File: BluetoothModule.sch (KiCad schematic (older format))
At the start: 21 parts, among them J8 SW_DIP_x01, J9 SW_DIP_x01, U17 BM64SPKS1MCx, U5 APX803L

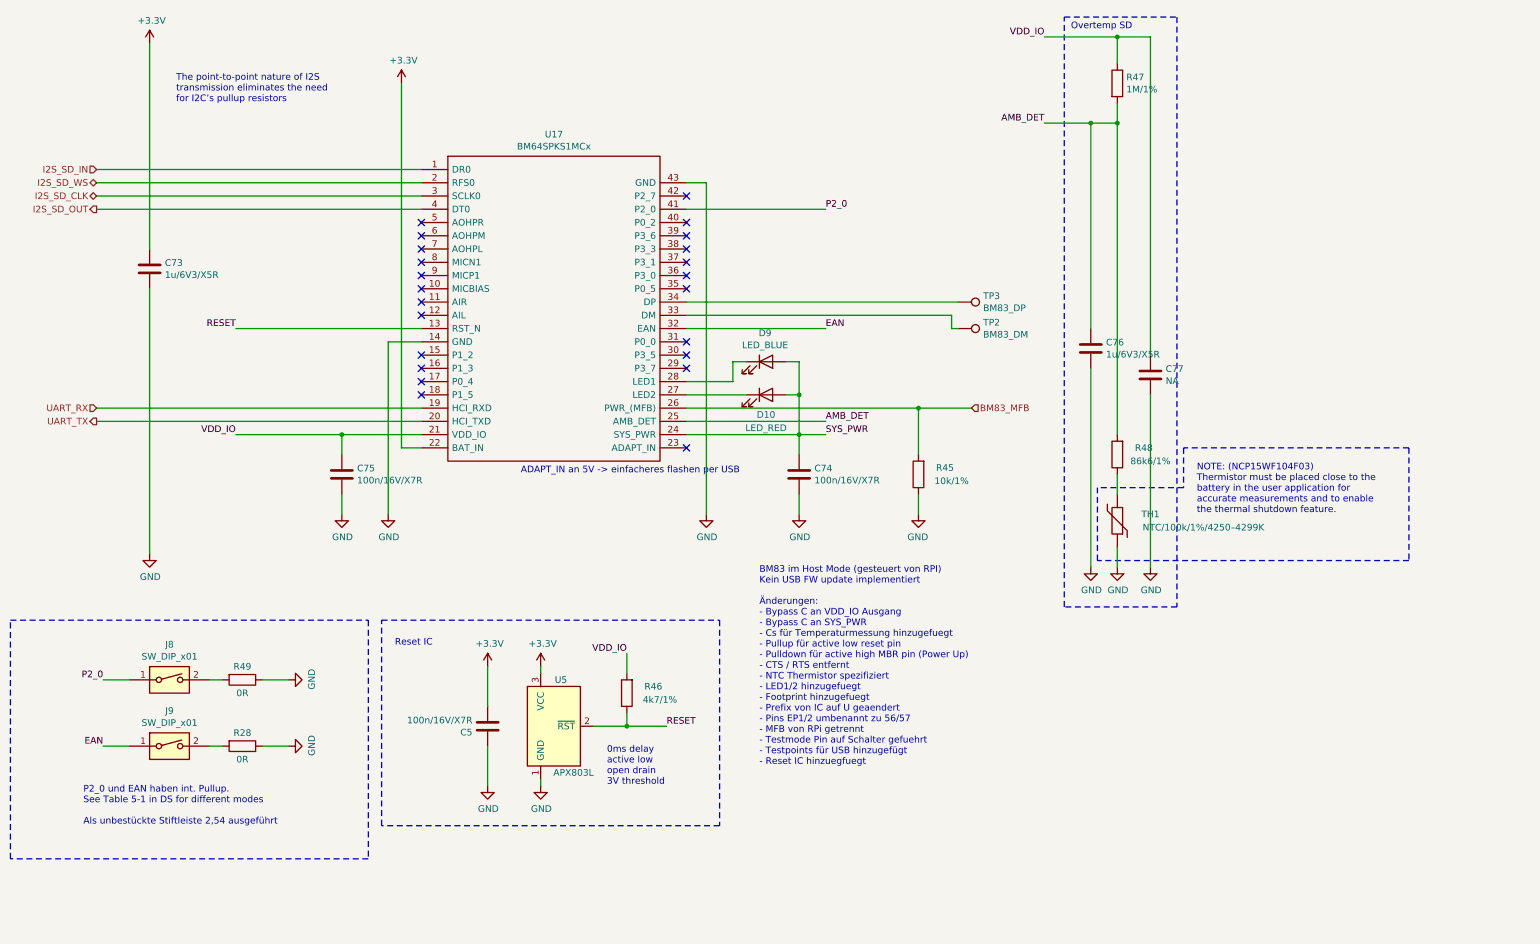
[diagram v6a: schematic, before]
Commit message: schematic changes up to layout import
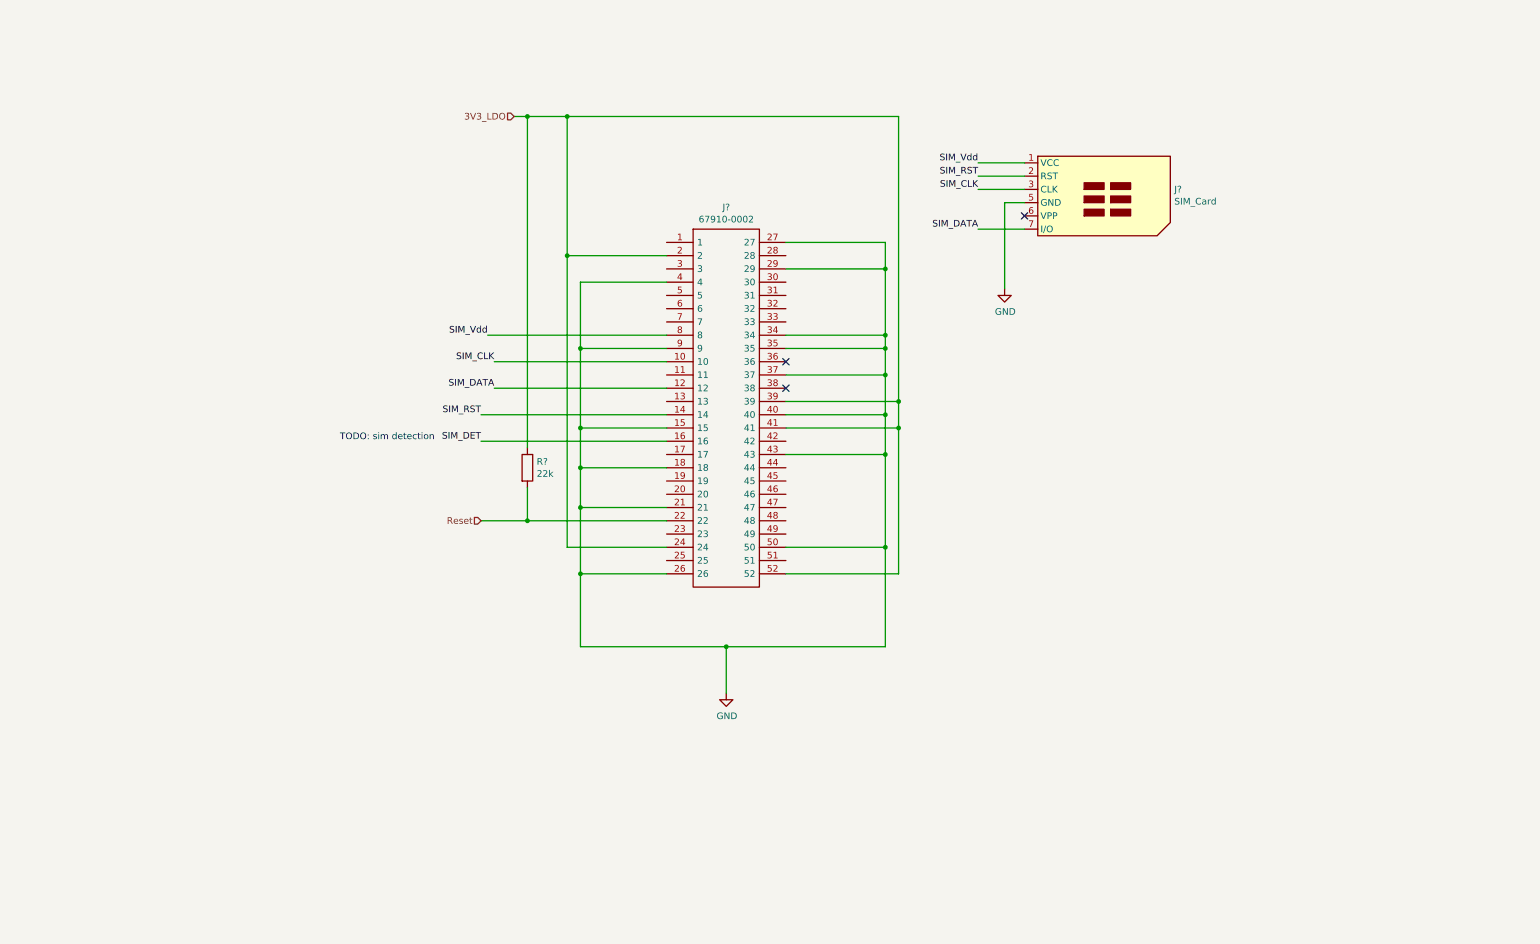
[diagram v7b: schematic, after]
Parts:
- removed C5, C74, C75: 100n/16V/X7R, Capacitor_SMD:C_0402_1005Metric, symbol Device:C
- removed C73, C76: 1u/6V3/X5R, Capacitor_SMD:C_0402_1005Metric, symbol Device:C
- removed C77: NA, Capacitor_SMD:C_0402_1005Metric, symbol Device:C
- removed D10: LED_RED, LED_SMD:LED_0603_1608Metric, symbol Device:LED
- removed D9: LED_BLUE, LED_SMD:LED_0603_1608Metric, symbol Device:LED
- removed J8, J9: SW_DIP_x01, Connector_PinHeader_2.54mm:PinHeader_1x02_P2.54mm_Vertical, symbol Switch:SW_DIP_x01
- removed R28, R49: 0R, Resistor_SMD:R_0603_1608Metric, symbol Device:R
- removed R45: 10k/1%, Resistor_SMD:R_0402_1005Metric, symbol Device:R
- removed R46: 4k7/1%, Resistor_SMD:R_0402_1005Metric, symbol Device:R
- removed R47: 1M/1%, Resistor_SMD:R_0402_1005Metric, symbol Device:R
- removed R48: 86k6/1%, Resistor_SMD:R_0402_1005Metric, symbol Device:R
- removed TH1: NTC/100k/1%/4250–4299K, Resistor_SMD:R_0603_1608Metric, symbol Device:Thermistor
- removed TP2: BM83_DM, TestPoint:TestPoint_Pad_D1.5mm, symbol Connector:TestPoint
- removed TP3: BM83_DP, TestPoint:TestPoint_Pad_D1.5mm, symbol Connector:TestPoint
- removed U17: BM64SPKS1MCx, TeKaDe:BM64, symbol TeKaDe:BM64SPKS1MCx
- removed U5: APX803L, Package_TO_SOT_SMD:SOT-23, symbol TeKaDe:APX803L
- added J?: 67910-0002, 67910-5700, symbol 67910-0002:67910-0002
- added J?: SIM_Card, Connector_JAE:JAE_SIM_Card_SF72S006, symbol Connector:SIM_Card
- added R?: 22k, symbol Device:R
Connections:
- net GND: now also J?.15, J?.18, J?.21, J?.26, J?.27, J?.29, J?.34, J?.35, J?.37, J?.4, J?.40, J?.43, J?.5 (GND), J?.50, J?.9
- new net 3V3_LDO: J?.2, J?.24, J?.39, J?.41, J?.52, R?.1
- new net Reset: J?.22, R?.2
- new net SIM_CLK: J?.10, J?.3 (CLK)
- new net SIM_DATA: J?.12, J?.7 (I/O)
- new net SIM_DET: J?.16
- new net SIM_RST: J?.14, J?.2 (RST)
- new net SIM_Vdd: J?.1 (VCC), J?.8
- no-connect marks 23 -> 3
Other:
- note added: "TODO: sim detection"
- note removed: "0ms delay\nactive low\nopen drain\n3V threshold"
- note removed: "ADAPT_IN an 5V -> einfacheres flashen per USB"
- note removed: "BM83 im Host Mode (gesteuert von RPI)\nKein USB FW update implementiert\n\nÄnderungen:\n- Bypass C an VDD_IO Ausgang\n- Bypass C an SYS_PWR\n- Cs für Temperaturmessung hinzugefuegt\n- Pullup für active low reset pin\n- Pulldown für active high MBR pin (Power Up)\n- CTS / RTS entfernt\n- NTC Thermistor spezifiziert\n- LED1/2 hinzugefuegt\n- Footprint hinzugefuegt\n- Prefix von IC auf U geaendert\n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"
- note removed: "NOTE: (NCP15WF104F03)\nThermistor must be placed close to the\nbattery in the user application for\naccurate measurements and to enable\nthe thermal shutdown feature."
- note removed: "Overtemp SD"
- note removed: "P2_0 und EAN haben int. Pullup.\nSee Table 5-1 in DS for different modes\n\nAls unbestückte Stiftleiste 2,54 ausgeführt"
- note removed: "Reset IC"
- note removed: "The point-to-point nature of I2S \ntransmission eliminates the need \nfor I2C’s pullup resistors"
